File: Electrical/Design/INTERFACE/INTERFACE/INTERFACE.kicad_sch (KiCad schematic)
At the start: 46 parts, among them J1 Conn_01x04, J3 Conn_01x04, J5 FFC_Conn_01x08_combine_pins2, J6 FFC_Conn_01x08_combine_pins2, Q3 WST2011, Q4 WST2011, U1 NUP4202W1T2G, U2 NUP4202W1T2G, U3 OH49E-S, U4 LMV321, U5 BL1551B, U6 BL1551B, U7 BL1551B, U8 BL1551B

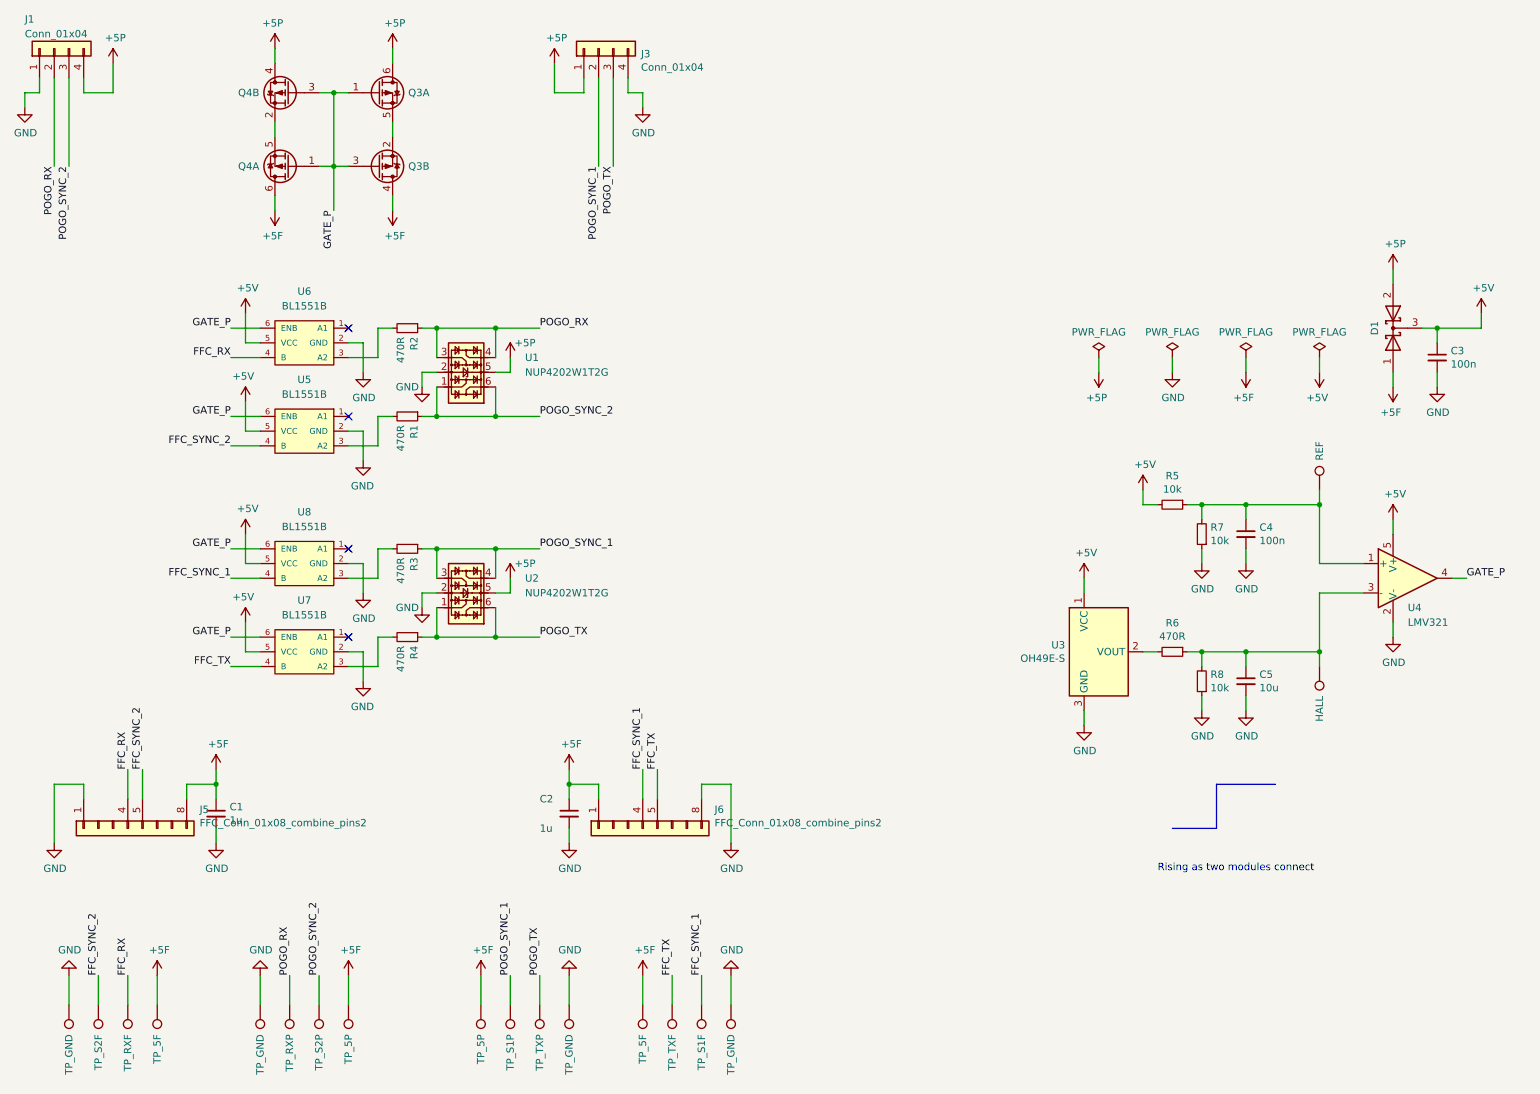
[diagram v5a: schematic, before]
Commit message: SUKU pogo-pin and battery-conn partnumbers added
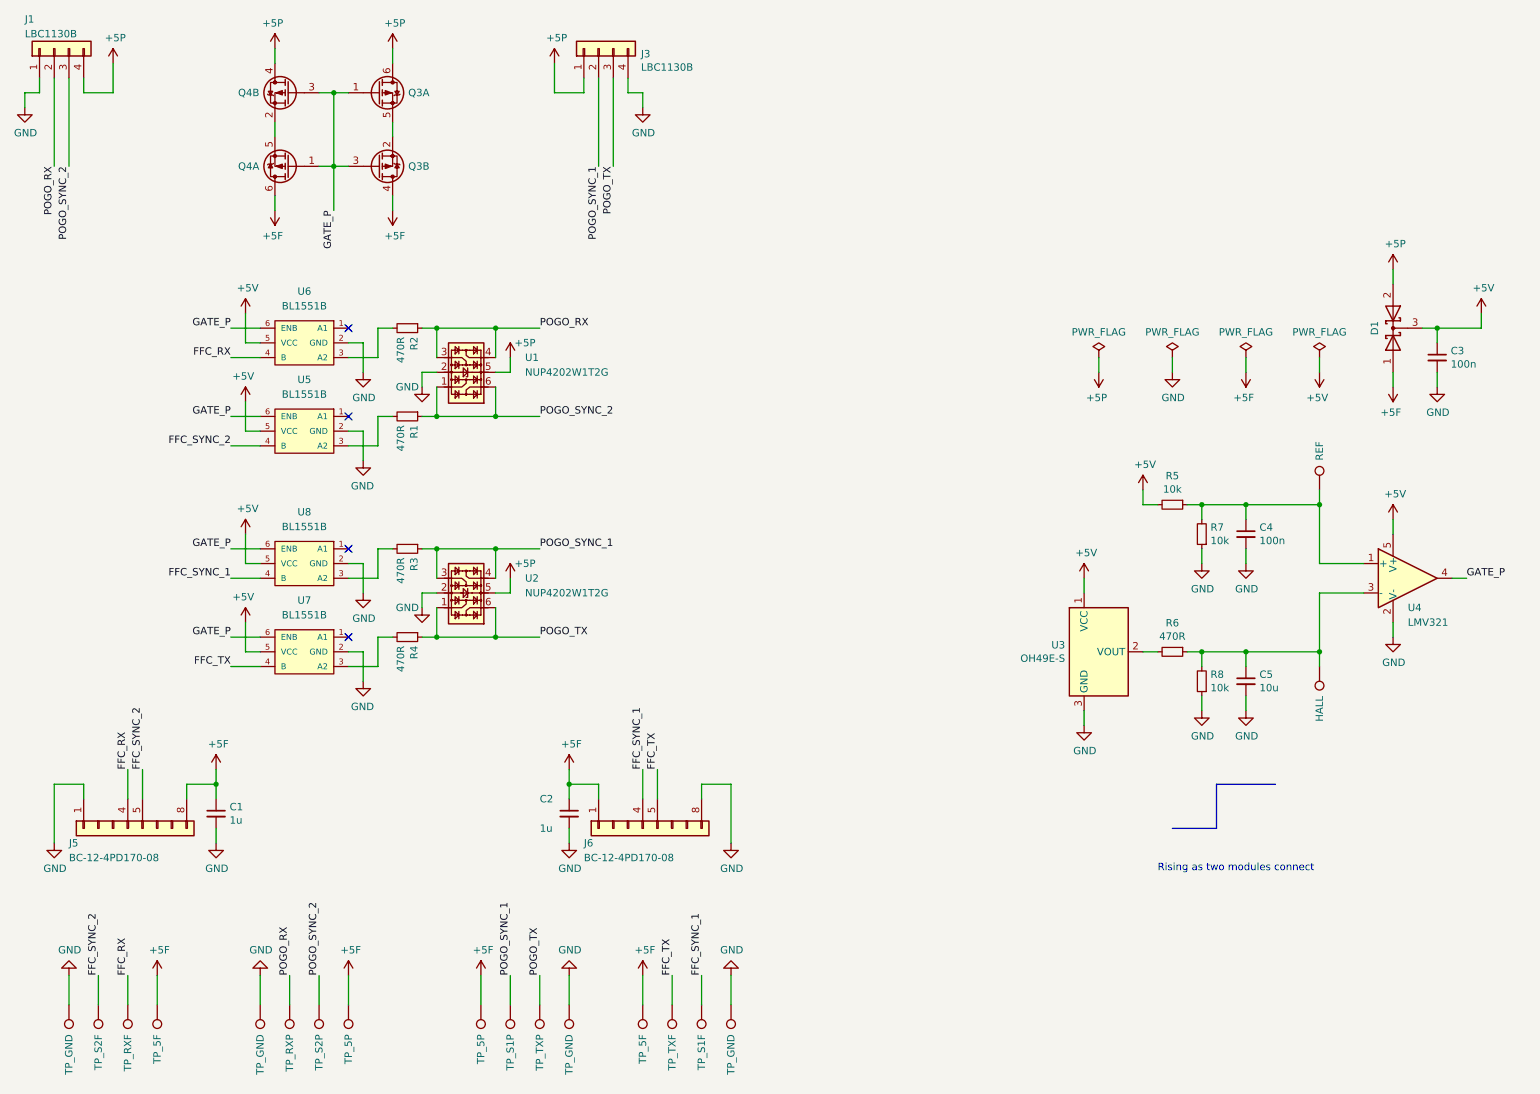
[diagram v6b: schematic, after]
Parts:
- J1, J3: value Conn_01x04 -> LBC1130B; Part N.F. -> LBC1130B
- J5, J6: value FFC_Conn_01x08_combine_pins2 -> BC-12-4PD170-08
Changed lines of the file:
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@@
       (effects (font (size 1.27 1.27)) (justify right))
     )
-    (property "Value" "Conn_01x04" (at 25.4 17.78 90)
+    (property "Value" "LBC1130B" (at 25.4 17.78 90)
       (effects (font (size 1.27 1.27)) (justify right))
     )
@@
       (effects (font (size 1.27 1.27)) hide)
     )
-    (property "Part" "N.F." (at 30.48 20.32 90)
+    (property "Part" "LBC1130B" (at 30.48 20.32 90)
       (effects (font (size 1.27 1.27)) hide)
     )
@@
       (effects (font (size 1.27 1.27)) (justify right))
     )
-    (property "Value" "Conn_01x04" (at 131.7752 23.5458 90)
+    (property "Value" "LBC1130B" (at 131.7752 23.5458 90)
       (effects (font (size 1.27 1.27)) (justify right))
     )
@@
       (effects (font (size 1.27 1.27)) hide)
     )
-    (property "Part" "N.F." (at 124.46 20.32 90)
+    (property "Part" "LBC1130B" (at 124.46 20.32 90)
       (effects (font (size 1.27 1.27)) hide)
     )
@@
   (symbol (lib_id "suku_basics:FFC_Conn_01x08_combine_pins2") (at 43.18 154.94 90) (mirror x) (unit 1)
     (in_bom yes) (on_board yes) (dnp no)
-    (property "Reference" "J5" (at 55.5752 151.6888 90)
+    (property "Reference" "J5" (at 33.02 157.48 90)
       (effects (font (size 1.27 1.27)) (justify right))
     )
-    (property "Value" "FFC_Conn_01x08_combine_pins2" (at 55.5752 154.0002 90)
+    (property "Value" "BC-12-4PD170-08" (at 33.02 160.02 90)
       (effects (font (size 1.27 1.27)) (justify right))
     )
@@
   (symbol (lib_id "suku_basics:FFC_Conn_01x08_combine_pins2") (at 132.08 154.94 90) (mirror x) (unit 1)
     (in_bom yes) (on_board yes) (dnp no)
-    (property "Reference" "J6" (at 144.4752 151.6888 90)
+    (property "Reference" "J6" (at 121.92 157.48 90)
       (effects (font (size 1.27 1.27)) (justify right))
     )
-    (property "Value" "FFC_Conn_01x08_combine_pins2" (at 144.4752 154.0002 90)
+    (property "Value" "BC-12-4PD170-08" (at 121.92 160.02 90)
       (effects (font (size 1.27 1.27)) (justify right))
     )

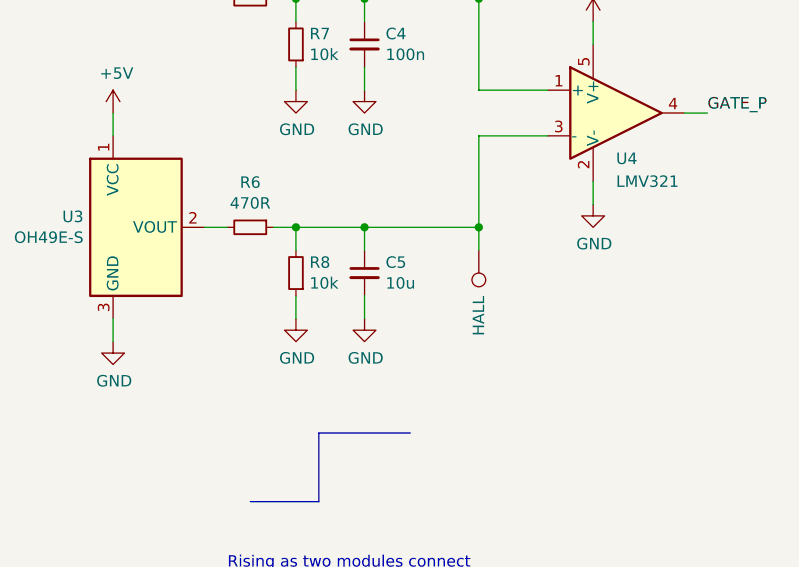
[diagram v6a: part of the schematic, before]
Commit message: SUKU interface passive component values consolidated for BOM optimization
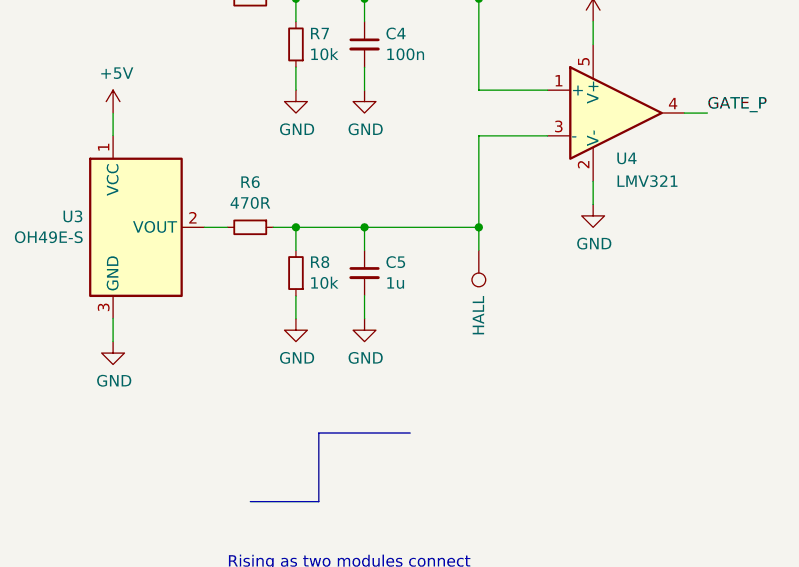
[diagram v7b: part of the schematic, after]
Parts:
- C5: value 10u -> 1u
- R6: footprint suku_basics:RES_0805 -> suku_basics:RES_0402
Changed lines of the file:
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@@
       (effects (font (size 1.27 1.27)))
     )
-    (property "Footprint" "suku_basics:RES_0805" (at 223.52 124.46 0)
+    (property "Footprint" "suku_basics:RES_0402" (at 223.52 124.46 0)
       (effects (font (size 1.27 1.27)) hide)
     )
@@
       (effects (font (size 1.27 1.27)) (justify left))
     )
-    (property "Value" "10u" (at 238.5568 130.683 0)
+    (property "Value" "1u" (at 238.5568 130.683 0)
       (effects (font (size 1.27 1.27)) (justify left))
     )
